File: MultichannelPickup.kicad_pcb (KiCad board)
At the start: 4 copper layers, 95 parts, among them J201 SWD Header, J301 BATT, Q201 BC847, Q202 BC847, Q203 BC847, SW201 RST, SW202 BOOT, SW203 SW_ADDR, SW301 PWR, U201 STM32H7B0VBTx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

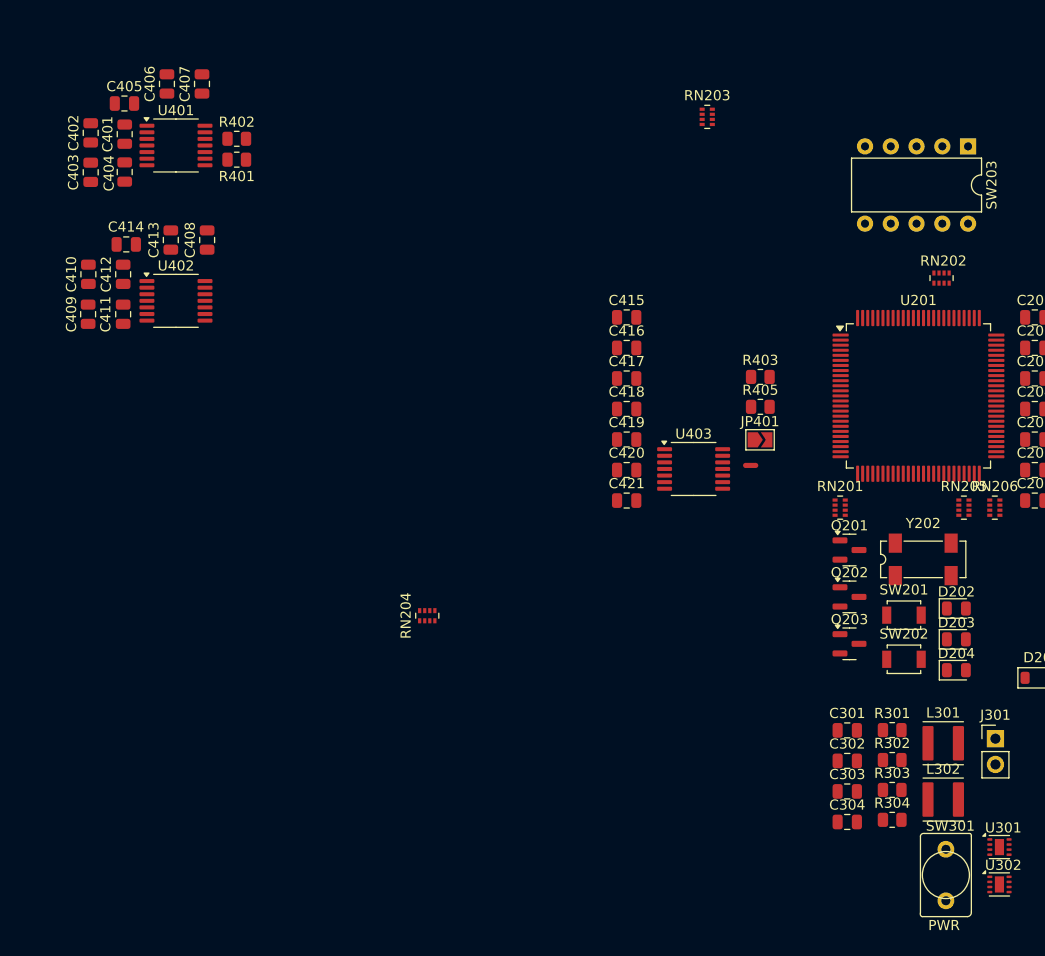
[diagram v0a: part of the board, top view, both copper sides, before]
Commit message: RF schematic drawn
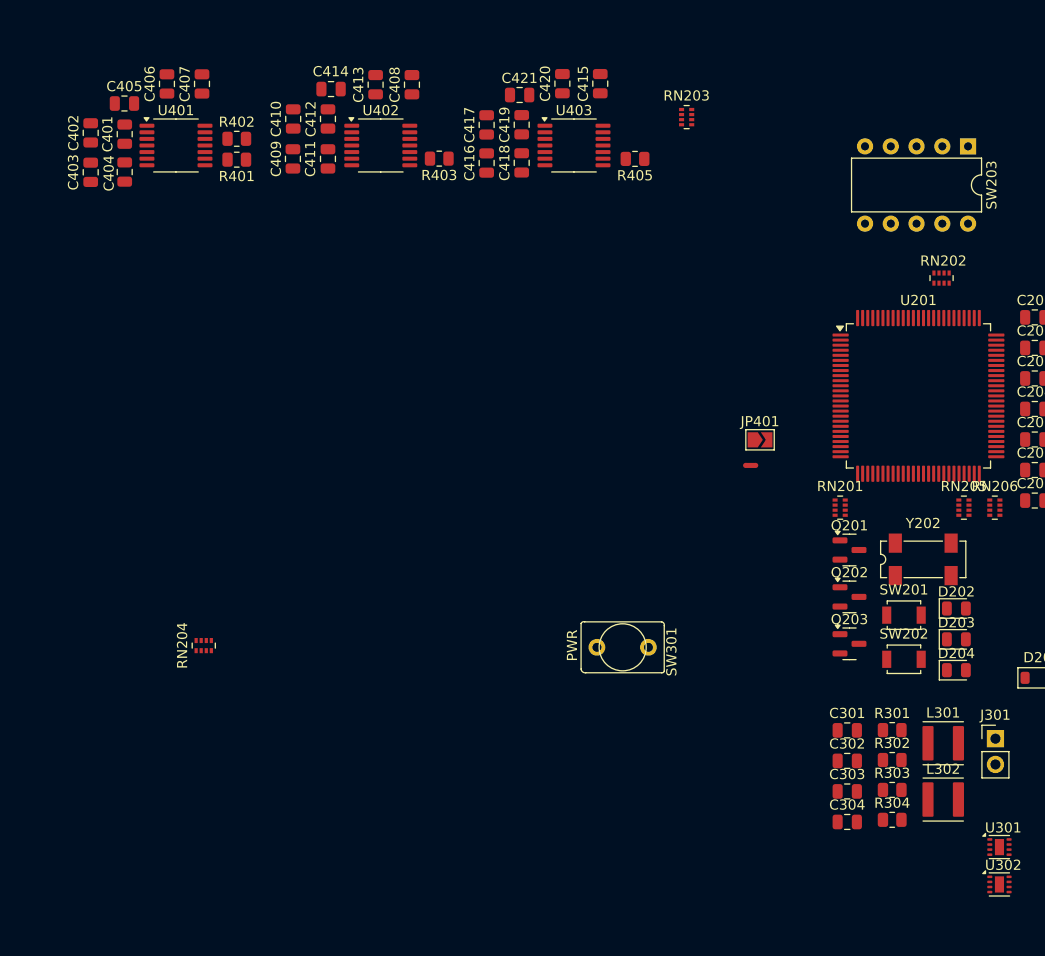
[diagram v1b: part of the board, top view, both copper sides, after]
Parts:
- moved C421 41.4 mm to (113.9, 51.1), turned to 180 degrees
- moved SW301 39.0 mm to (124.1, 105.5), turned to -90 degrees
- moved C420 38.6 mm to (118.2, 49.9), turned to 90 degrees
- moved R403 38.3 mm to (106.0, 57.3), turned to 180 degrees
- moved U403 34.0 mm to (119.3, 56.0)
- moved C419 32.7 mm to (114.1, 54.0), turned to 90 degrees
- moved C417 28.6 mm to (110.7, 54.0), turned to 90 degrees
- moved R405 27.4 mm to (125.3, 57.4), turned to 180 degrees
- moved C418 26.4 mm to (114.1, 57.7), turned to -90 degrees
- moved C408 25.3 mm to (103.3, 50.0)
- moved C413 25.3 mm to (99.7, 50.0)
- moved C414 25.3 mm to (95.4, 50.5)
- moved U402 25.3 mm to (100.3, 56.0)
- moved C409 25.3 mm to (91.6, 57.4)
- moved C410 25.3 mm to (91.6, 53.4)
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
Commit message: op amp input stage
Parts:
- added C219: 10u, Capacitor_SMD:C_0805_2012Metric, F.Cu at (218.1, 90.0)
- added C220: 10u, Capacitor_SMD:C_0805_2012Metric, F.Cu at (218.1, 93.0)
- added C221: 100n, Capacitor_SMD:C_0805_2012Metric, F.Cu at (218.1, 96.0)
- added FB202: 90R, Resistor_SMD:R_0805_2012Metric, F.Cu at (218.1, 99.0)
- added R208: 15k, Resistor_SMD:R_0805_2012Metric, F.Cu at (218.1, 102.0)
- added RN207: 47R, Resistor_SMD:R_Array_Concave_4x0402, F.Cu at (217.4, 105.2)
- added U202: RYLR689, RF_Module:RYLR689, F.Cu at (197.1, 89.3)
- RN201, RN202, RN203, RN204, RN205, RN206: footprint Resistor_SMD:R_Array_Concave_4x0402 -> Resistor_SMD:R_Array_Concave_4x0603
- moved NT401 199.7 mm to (-0.66, -57.4)
- moved RN204 87.2 mm to (161.3, 67.4), turned to -90 degrees
- moved RN203 31.4 mm to (100.0, 61.0), turned to -90 degrees
- moved RN202 1.69 mm to (155.9, 67.5)
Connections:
- net Net-(RN202-R1.1) renamed /MasterMCU/FREQ2
- net Net-(RN202-R2.1) renamed /MasterMCU/FREQ1
- net Net-(RN205-R2.1) renamed /MasterMCU/LED3
- net Net-(RN205-R3.1) renamed /MasterMCU/LED2
- net Net-(RN205-R4.1) renamed /MasterMCU/LED1
- R205 pad 1: LORA_SCK -> LORA_CS
- RN201 pad 1: unconnected-(RN201-R1.1-Pad1) -> BCK_A
- RN201 pad 3: BCK_A -> unconnected-(RN201-R3.1-Pad3)
- RN201 pad 6: /MasterMCU/CK_1 -> unconnected-(RN201-R3.2-Pad6)
- RN201 pad 8: unconnected-(RN201-R1.2-Pad8) -> /MasterMCU/CK_1
- RN203 pad 1: unconnected-(RN203-R1.1-Pad1) -> BCK_B
- RN203 pad 3: BCK_B -> unconnected-(RN203-R3.1-Pad3)
- RN203 pad 6: /MasterMCU/CK_2 -> unconnected-(RN203-R3.2-Pad6)
- RN203 pad 8: unconnected-(RN203-R1.2-Pad8) -> /MasterMCU/CK_2
- RN204 pad 1: unconnected-(RN204-R1.1-Pad1) -> BCK_C
- RN204 pad 3: BCK_C -> unconnected-(RN204-R3.1-Pad3)
- RN204 pad 6: /MasterMCU/CK_3 -> unconnected-(RN204-R3.2-Pad6)
- RN204 pad 8: unconnected-(RN204-R1.2-Pad8) -> /MasterMCU/CK_3
- U201 pad 15: unconnected-(U201-PC0-Pad15) -> LORA_RX_ENABLE
- U201 pad 16: unconnected-(U201-PC1-Pad16) -> LORA_TX_ENABLE
- U201 pad 96: unconnected-(U201-PB9-Pad96) -> LORA_IO2

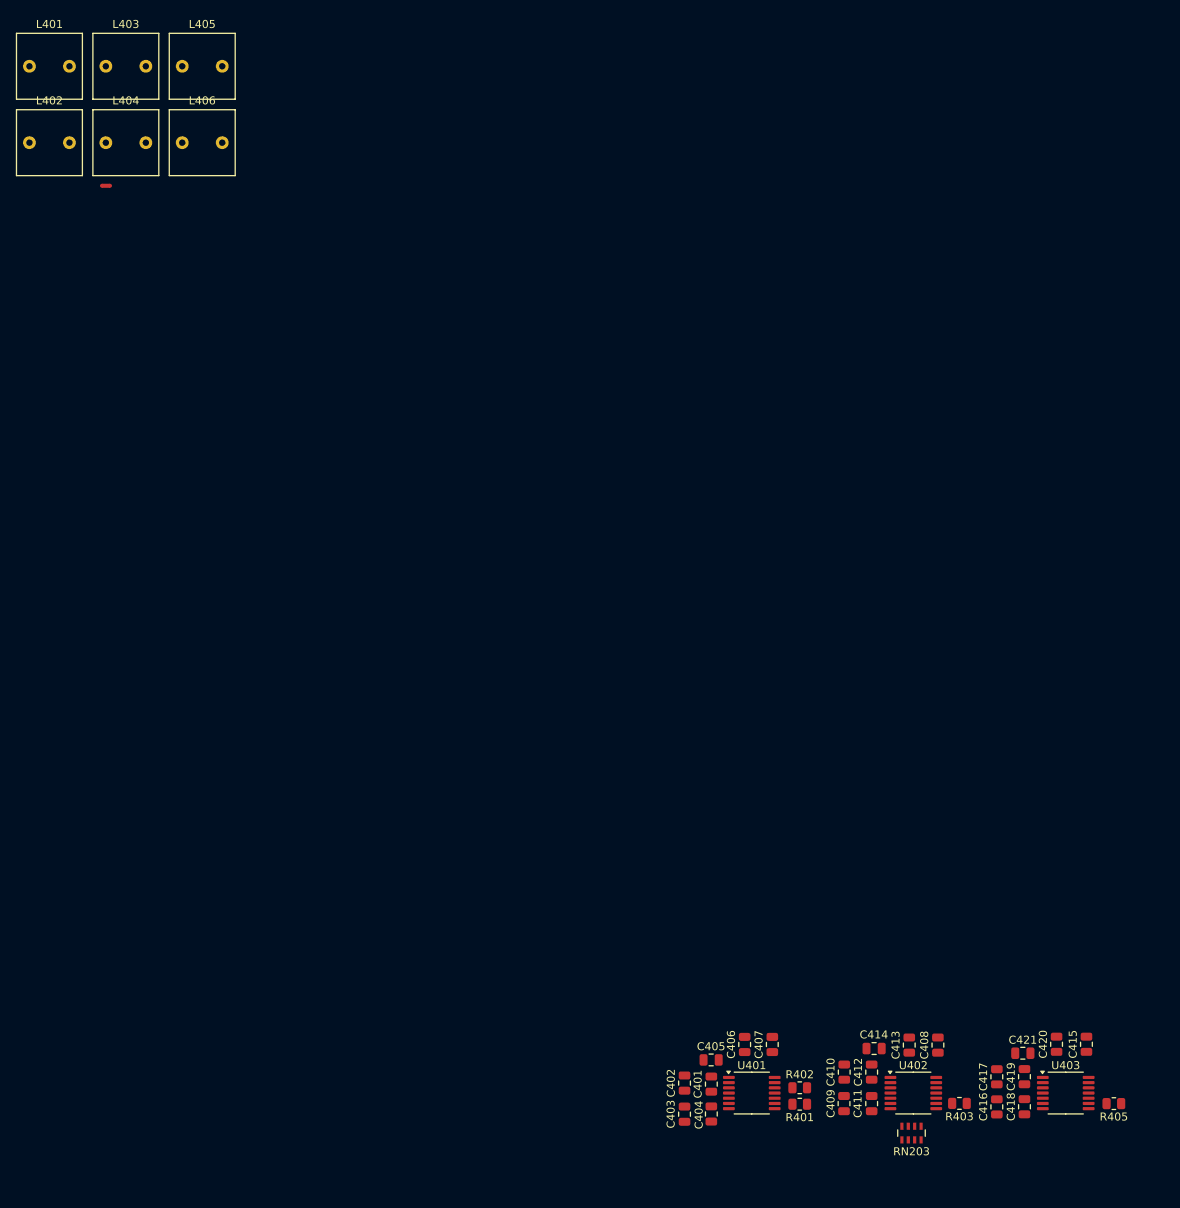
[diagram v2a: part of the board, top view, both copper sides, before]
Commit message: resistor array routing fix
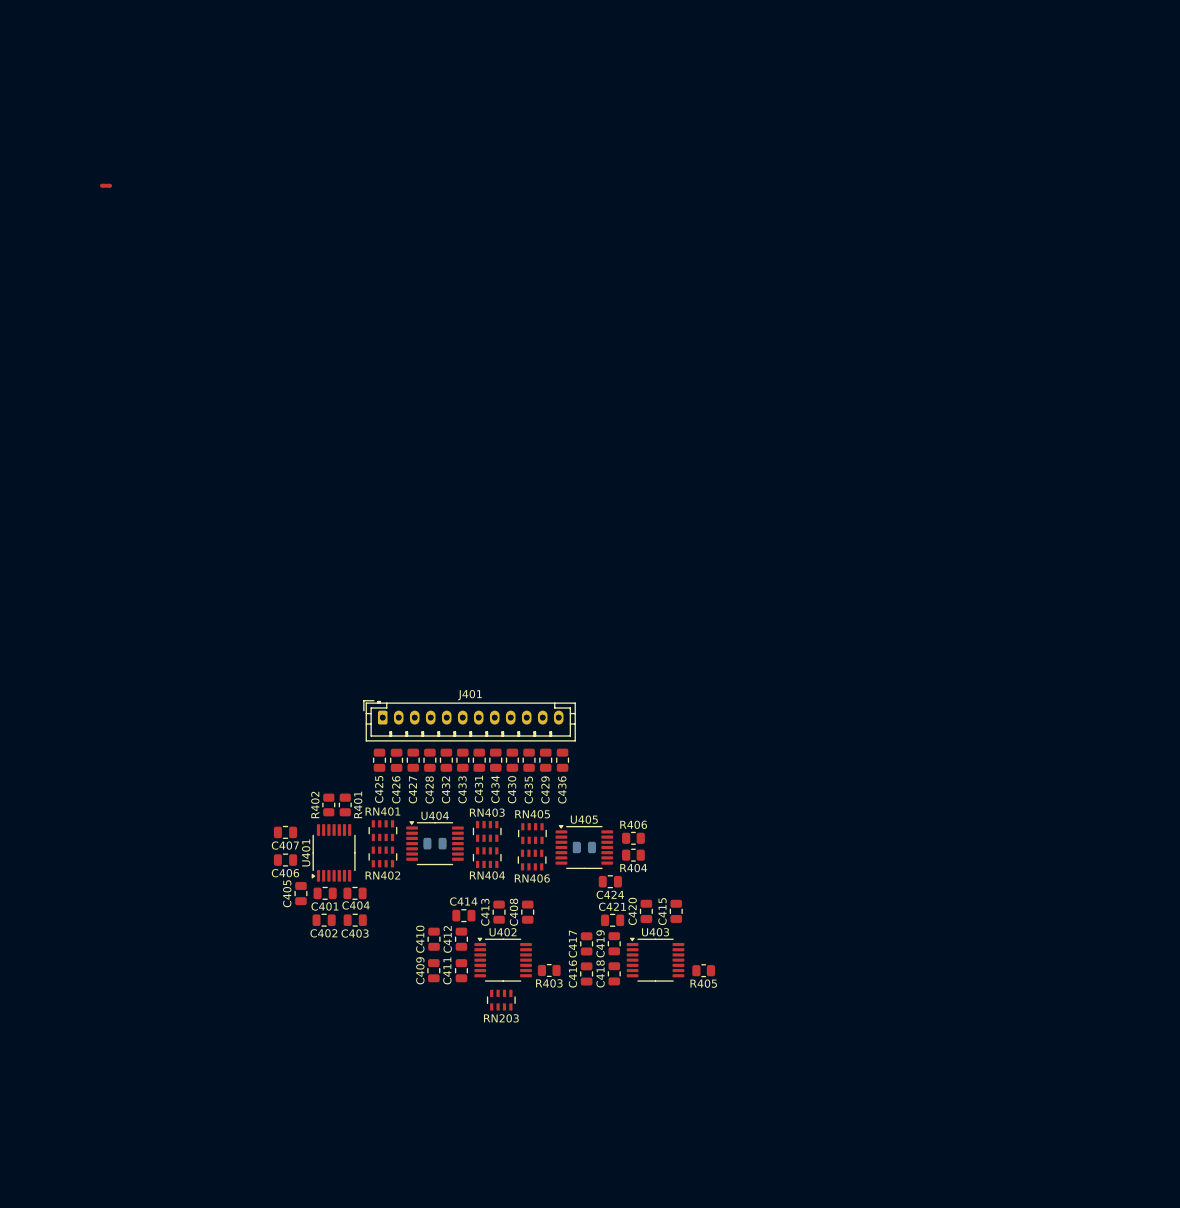
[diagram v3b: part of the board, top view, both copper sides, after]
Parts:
- removed L401, L402, L403, L404, L405, L406: 7000 winds, Inductor_THT:L_Radial_L8.0mm_W8.0mm_P5.00mm_Neosid_SD8
- added C422: 100n, Capacitor_SMD:C_0805_2012Metric, B.Cu at (40.5, 24.9)
- added C423: 100n, Capacitor_SMD:C_0805_2012Metric, B.Cu at (59.1, 25.3)
- added C424: 100n, Capacitor_SMD:C_0805_2012Metric, F.Cu at (62.4, 29.6)
- added C425: 1u, Capacitor_SMD:C_0805_2012Metric, F.Cu at (33.5, 14.4)
- added C426: 1u, Capacitor_SMD:C_0805_2012Metric, F.Cu at (35.7, 14.4)
- added C427: 1u, Capacitor_SMD:C_0805_2012Metric, F.Cu at (37.7, 14.4)
- added C428: 1u, Capacitor_SMD:C_0805_2012Metric, F.Cu at (39.8, 14.4)
- added C429: 1u, Capacitor_SMD:C_0805_2012Metric, F.Cu at (54.3, 14.4)
- added C430: 1u, Capacitor_SMD:C_0805_2012Metric, F.Cu at (50.1, 14.4)
- added C431: 1u, Capacitor_SMD:C_0805_2012Metric, F.Cu at (46.0, 14.4)
- added C432: 1u, Capacitor_SMD:C_0805_2012Metric, F.Cu at (41.9, 14.4)
- added C433: 1u, Capacitor_SMD:C_0805_2012Metric, F.Cu at (43.9, 14.4)
- added C434: 1u, Capacitor_SMD:C_0805_2012Metric, F.Cu at (48.1, 14.4)
- added C435: 1u, Capacitor_SMD:C_0805_2012Metric, F.Cu at (52.2, 14.4)
- added C436: 1u, Capacitor_SMD:C_0805_2012Metric, F.Cu at (56.4, 14.4)
- added J401: Pickup, Connector_JST:JST_PH_B12B-PH-K_1x12_P2.00mm_Vertical, F.Cu at (33.9, 9.10)
- added R404: 100k, Resistor_SMD:R_0805_2012Metric, F.Cu at (65.3, 26.3)
- added R406: 100k, Resistor_SMD:R_0805_2012Metric, F.Cu at (65.3, 24.2)
- added RN401: 10k, Resistor_SMD:R_Array_Concave_4x0603, F.Cu at (34.0, 23.2)
- added RN402: 33k, Resistor_SMD:R_Array_Concave_4x0603, F.Cu at (34.0, 26.5)
- added RN403: 10k, Resistor_SMD:R_Array_Concave_4x0603, F.Cu at (47.0, 23.3)
- added RN404: 33k, Resistor_SMD:R_Array_Concave_4x0603, F.Cu at (47.0, 26.6)
- added RN405: 10k, Resistor_SMD:R_Array_Concave_4x0603, F.Cu at (52.6, 23.6)
- added RN406: 33k, Resistor_SMD:R_Array_Concave_4x0603, F.Cu at (52.6, 26.9)
- added U404: MCP6009, Package_SO:TSSOP-14_4.4x5mm_P0.65mm, F.Cu at (40.5, 24.9)
- added U405: MCP6009, Package_SO:TSSOP-14_4.4x5mm_P0.65mm, F.Cu at (59.1, 25.3)
- NT401: value COIL_GND -> VGD
- moved R402 68.7 mm to (27.2, 20.0), turned to 90 degrees
- moved R401 68.0 mm to (29.2, 20.0), turned to -90 degrees
- moved C407 66.4 mm to (21.8, 23.5), turned to 180 degrees
- moved C406 61.9 mm to (21.8, 26.9), turned to 180 degrees
- moved U401 60.2 mm to (27.8, 26.0), turned to 90 degrees
- moved C405 55.3 mm to (23.7, 31.1), turned to -90 degrees
- moved C410 53.9 mm to (40.3, 36.8)
- moved C411 53.9 mm to (43.8, 40.7)
- moved C412 53.9 mm to (43.8, 36.8)
- moved C421 53.9 mm to (62.7, 34.4)
- moved C409 53.9 mm to (40.3, 40.7)
- moved C418 53.9 mm to (62.9, 41.1)
- moved C419 53.9 mm to (62.9, 37.4)
- moved R403 53.9 mm to (54.7, 40.7)
- moved R405 53.9 mm to (74.0, 40.7)
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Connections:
- NT401 pad 1: /Pickup/COIL_COM -> /Pickup/VGND
- NT401 pad 2: GND -> Net-(U405D--)
